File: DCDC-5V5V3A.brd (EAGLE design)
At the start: 40 x 24 mm, 33 parts, among them U1 TPS63020DSJR

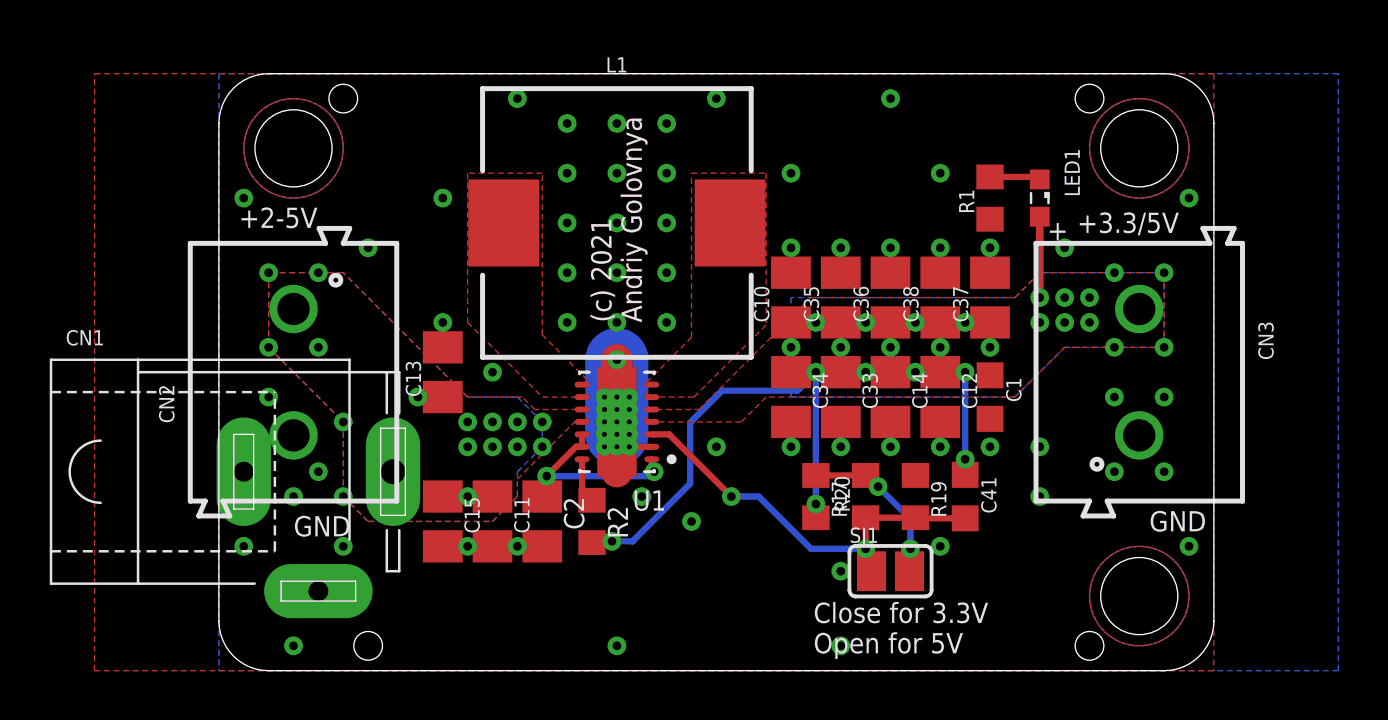
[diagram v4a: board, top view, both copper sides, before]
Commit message: Added 200k resistor to improve voltage output. Generated CAM files. Generated PNG preview. Generated PDF schematics. Adjusted BoM and PnP files. Adjusted Excel calculator.
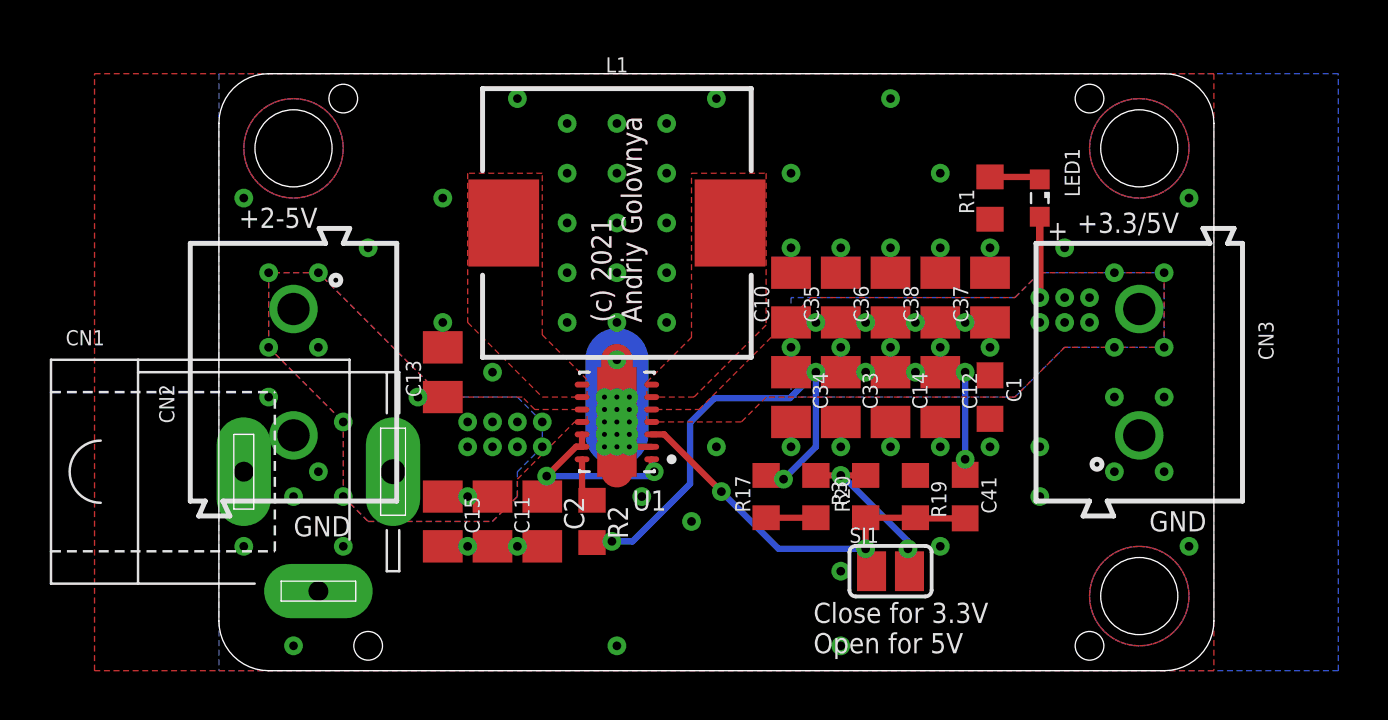
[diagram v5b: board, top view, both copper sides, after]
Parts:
- added R3: 20k, rcl:R0603
- moved R17 2.00 mm to (22.0, 7.00), turned to 90 degrees
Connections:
- new net N$3: R20.2, R3.1, SJ1.2
- net N$2: now also R3.2; no longer R20.2, SJ1.2
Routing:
- net N$3: track 0.00 -> 7.02 mm, vias 0 -> 2
- net N$2: track 6.64 -> 2.00 mm, vias 2 -> 0
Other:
- board text added: "DCDC-5V5V3A-0011"
- board text removed: "DCDC-5V5V3A-0010"
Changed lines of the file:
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@@
 <hole x="37" y="21" drill="3.1"/>
 <hole x="37" y="3" drill="3.1"/>
-<text x="33" y="20" size="1.6764" layer="22" font="vector" ratio="20" rot="MR0">DCDC-5V5V3A-0010</text>
+<text x="33" y="20" size="1.6764" layer="22" font="vector" ratio="20" rot="MR0">DCDC-5V5V3A-0011</text>
 <text x="0.8" y="17.8" size="0.8128" layer="21" font="vector">+2-5V</text>
 <text x="3" y="5.4" size="0.8128" layer="21" font="vector">GND</text>
@@
 <attribute name="VALUE" x="12.5" y="10.95" size="0.6096" layer="27" font="vector"/>
 </element>
-<element name="R17" library="rcl" library_urn="urn:adsk.eagle:library:334" package="R0603" package3d_urn="urn:adsk.eagle:package:23555/3" value="1M" x="24" y="7" smashed="yes" rot="R270">
-<attribute name="NAME" x="24.635" y="7.635" size="0.6096" layer="25" font="vector" rot="R270"/>
-<attribute name="POPULARITY" value="70" x="-19.18" y="-29.83" size="1.778" layer="27" rot="R270" display="off"/>
-<attribute name="SPICEPREFIX" value="R" x="-19.18" y="-29.83" size="1.778" layer="27" rot="R270" display="off"/>
-<attribute name="VALUE" x="22.095" y="7.635" size="0.6096" layer="27" font="vector" rot="R270"/>
+<element name="R17" library="rcl" library_urn="urn:adsk.eagle:library:334" package="R0603" package3d_urn="urn:adsk.eagle:package:23555/3" value="1M" x="22" y="7" smashed="yes" rot="R90">
+<attribute name="NAME" x="21.365" y="6.365" size="0.6096" layer="25" font="vector" rot="R90"/>
+<attribute name="POPULARITY" value="70" x="65.18" y="43.83" size="1.778" layer="27" rot="R90" display="off"/>
+<attribute name="SPICEPREFIX" value="R" x="65.18" y="43.83" size="1.778" layer="27" rot="R90" display="off"/>
+<attribute name="VALUE" x="23.905" y="6.365" size="0.6096" layer="27" font="vector" rot="R90"/>
 </element>
 <element name="R19" library="rcl" library_urn="urn:adsk.eagle:library:334" package="R0603" package3d_urn="urn:adsk.eagle:package:23555/3" value="180k" x="28" y="7" smashed="yes" rot="R270">
@@
 </element>
 <element name="HOLE4" library="_my_fiducia" package="TOOLING-HOLE" value="TOOLINGHOLE" x="6" y="1" smashed="yes"/>
+<element name="R3" library="rcl" library_urn="urn:adsk.eagle:library:334" package="R0603" package3d_urn="urn:adsk.eagle:package:23555/3" value="20k" x="24" y="7" smashed="yes" rot="R270">
+<attribute name="NAME" x="24.635" y="7.635" size="0.6096" layer="25" font="vector" rot="R270"/>
+<attribute name="POPULARITY" value="70" x="24" y="7" size="1.778" layer="27" rot="R270" display="off"/>
+<attribute name="SPICEPREFIX" value="R" x="24" y="7" size="1.778" layer="27" rot="R270" display="off"/>
+<attribute name="VALUE" x="22.095" y="7.635" size="0.6096" layer="27" font="vector" rot="R270"/>
+</element>
 </elements>
 <signals>
@@
 <vertex x="12.7" y="10.5"/>
 <vertex x="12.2" y="11"/>
-<vertex x="10" y="11"/>
-<vertex x="5" y="16"/>
+<vertex x="9" y="11"/>
+<vertex x="4" y="16"/>
 </polygon>
 <polygon width="0.3048" layer="16" thermals="no">
@@
 <vertex x="13" y="10"/>
 <vertex x="12" y="11"/>
-<vertex x="10" y="11"/>
-<vertex x="5" y="16"/>
+<vertex x="9" y="11"/>
+<vertex x="4" y="16"/>
 </polygon>
 <via x="4" y="16" extent="1-16" drill="0.35"/>
@@
 <wire x1="30" y1="8.5" x2="30" y2="12" width="0.254" layer="16"/>
 <via x="30" y="12" extent="1-16" drill="0.35"/>
-<wire x1="24" y1="6.15" x2="24" y2="6.7" width="0.254" layer="1"/>
-<via x="24" y="6.7" extent="1-16" drill="0.35"/>
-<wire x1="24" y1="6.7" x2="24" y2="12" width="0.254" layer="16"/>
+<via x="22.7" y="7.7" extent="1-16" drill="0.35"/>
+<wire x1="24" y1="9" x2="24" y2="12" width="0.254" layer="16"/>
+<wire x1="24" y1="9" x2="22.7" y2="7.7" width="0.254" layer="16"/>
 <via x="24" y="12" extent="1-16" drill="0.35"/>
 <via x="24" y="14" extent="1-16" drill="0.35"/>
@@
 </polygon>
 <via x="15.8" y="5.2" extent="1-16" drill="0.35"/>
-<wire x1="20.2276125" y1="11.2576" x2="18.9424" y2="9.9723875" width="0.254" layer="16"/>
-<wire x1="24" y1="12" x2="23.2576" y2="11.2576" width="0.254" layer="16"/>
+<wire x1="19.9276125" y1="10.9576" x2="18.9424" y2="9.9723875" width="0.254" layer="16"/>
+<wire x1="24" y1="12" x2="22.9576" y2="10.9576" width="0.254" layer="16"/>
 <wire x1="18.9424" y1="7.5124125" x2="16.6299875" y2="5.2" width="0.254" layer="16"/>
 <wire x1="16.6299875" y1="5.2" x2="15.8" y2="5.2" width="0.254" layer="16"/>
-<wire x1="23.2576" y1="11.2576" x2="20.2276125" y2="11.2576" width="0.254" layer="16"/>
+<wire x1="22.9576" y1="10.9576" x2="19.9276125" y2="10.9576" width="0.254" layer="16"/>
 <wire x1="18.9424" y1="9.9723875" x2="18.9424" y2="7.5124125" width="0.254" layer="16"/>
 <wire x1="15.8" y1="5.2" x2="15.75" y2="5.15" width="0.254" layer="1"/>
@@
 <via x="36" y="16" extent="1-16" drill="0.35"/>
 <via x="36" y="13" extent="1-16" drill="0.35"/>
+<wire x1="22" y1="7.85" x2="22.55" y2="7.85" width="0.254" layer="1"/>
+<wire x1="22.55" y1="7.85" x2="22.7" y2="7.7" width="0.254" layer="1"/>
 </signal>
 <signal name="FB">
@@
 <wire x1="26" y1="4.9" x2="26" y2="4.238" width="0.254" layer="1"/>
 <wire x1="26" y1="4.238" x2="26.238" y2="4" width="0.254" layer="1"/>
-<wire x1="17.4" y1="9.5" x2="18.1" y2="9.5" width="0.254" layer="1"/>
-<wire x1="18.1" y1="9.5" x2="20.6" y2="7" width="0.254" layer="1"/>
-<via x="20.6" y="7" extent="1-16" drill="0.35"/>
-<wire x1="23.8" y1="4.9" x2="21.7" y2="7" width="0.254" layer="16"/>
-<wire x1="20.6" y1="7" x2="21.7" y2="7" width="0.254" layer="16"/>
-<wire x1="26" y1="4.9" x2="23.8" y2="4.9" width="0.254" layer="16"/>
+<wire x1="17.4" y1="9.5" x2="17.9" y2="9.5" width="0.254" layer="1"/>
+<wire x1="17.9" y1="9.5" x2="20.2" y2="7.2" width="0.254" layer="1"/>
+<via x="20.2" y="7.2" extent="1-16" drill="0.35"/>
+<wire x1="22.5" y1="4.9" x2="20.2" y2="7.2" width="0.254" layer="16"/>
+<wire x1="26" y1="4.9" x2="22.5" y2="4.9" width="0.254" layer="16"/>
 <via x="26" y="4.9" extent="1-16" drill="0.35"/>
 </signal>
@@
 <signal name="N$2">
 <contactref element="R17" pad="1"/>
+<contactref element="R3" pad="2"/>
+<wire x1="24" y1="6.15" x2="22" y2="6.15" width="0.254" layer="1"/>
+</signal>
+<signal name="N$3">
 <contactref element="R20" pad="2"/>
+<contactref element="R3" pad="1"/>
 <contactref element="SJ1" pad="2"/>
-<wire x1="24" y1="7.85" x2="26" y2="7.85" width="0.254" layer="1"/>
-<wire x1="26" y1="7.85" x2="26.45" y2="7.4" width="0.254" layer="1"/>
-<wire x1="26.45" y1="7.4" x2="26.5" y2="7.4" width="0.254" layer="1"/>
-<via x="26.5" y="7.4" extent="1-16" drill="0.35"/>
-<wire x1="26.5" y1="7.4" x2="27.8" y2="6.1" width="0.254" layer="16"/>
-<wire x1="27.8" y1="6.1" x2="27.8" y2="4.9" width="0.254" layer="16"/>
-<via x="27.8" y="4.9" extent="1-16" drill="0.35"/>
-<wire x1="27.8" y1="4.9" x2="27.8" y2="4.038" width="0.254" layer="1"/>
-<wire x1="27.8" y1="4.038" x2="27.762" y2="4" width="0.254" layer="1"/>
+<wire x1="26" y1="7.85" x2="25" y2="7.85" width="0.254" layer="1"/>
+<wire x1="25" y1="7.85" x2="24" y2="7.85" width="0.254" layer="1"/>
+<wire x1="27.762" y1="4" x2="27.762" y2="4.838" width="0.254" layer="1"/>
+<wire x1="27.762" y1="4.838" x2="27.7" y2="4.9" width="0.254" layer="1"/>
+<via x="27.7" y="4.9" extent="1-16" drill="0.35"/>
+<via x="25" y="7.85" extent="1-16" drill="0.35"/>
+<wire x1="27.7" y1="4.9" x2="27.7" y2="5.2" width="0.254" layer="16"/>
+<wire x1="27.7" y1="5.2" x2="25.05" y2="7.85" width="0.254" layer="16"/>
+<wire x1="25" y1="7.85" x2="25.05" y2="7.85" width="0.254" layer="16"/>
 </signal>
 </signals>
